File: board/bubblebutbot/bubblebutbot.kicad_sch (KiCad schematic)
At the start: 23 parts, among them J1 Screw_Terminal_01x02, J2 Screw_Terminal_01x02, J3 Conn_01x06_Female, J4 Conn_01x06_Female, J5 Screw_Terminal_01x02, J6 Screw_Terminal_01x02, Q1 FDN336P, U1 WeMos_D1_mini, U3 TPS613222ADBV

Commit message: gerber for 1v01 ready
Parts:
- removed J1, J2, J5, J6: Screw_Terminal_01x02, TerminalBlock:TerminalBlock_bornier-2_P5.08mm, symbol Connector:Screw_Terminal_01x02
- added J1, J2: Screw_Terminal_01x04, TerminalBlock_MetzConnect:TerminalBlock_MetzConnect_Type094_RT03504HBLU_1x04_P5.00mm_Horizontal, symbol Connector:Screw_Terminal_01x04
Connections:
- net GND: now also J1.1 (Pin_1)
- net SERVO_PWM: now also J1.3 (Pin_3)
- net SPLY: now also J1.4 (Pin_4)
- net at L1.1, R3.1: now also J1.2 (Pin_2)
- net at J3.3 (Pin_3): now also J2.3 (Pin_3)
- net at J3.2 (Pin_2): now also J2.4 (Pin_4)
- net at J3.4 (Pin_4): now also J2.2 (Pin_2)
- net at J3.5 (Pin_5): now also J2.1 (Pin_1)

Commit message: first steps into the final prod pcb!
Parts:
- removed C4: 10u, Capacitor_SMD:C_0603_1608Metric_Pad1.08x0.95mm_HandSolder, symbol Device:C
- removed D1: SS14, Diode_SMD:D_SMA, symbol Device:D_Schottky
- removed D3: LED, LED_SMD:LED_0603_1608Metric_Pad1.05x0.95mm_HandSolder, symbol Device:LED
- removed J1, J2: Screw_Terminal_01x04, TerminalBlock_MetzConnect:TerminalBlock_MetzConnect_Type094_RT03504HBLU_1x04_P5.00mm_Horizontal, symbol Connector:Screw_Terminal_01x04
- removed J3, J4: Conn_01x06_Female, Connector_PinSocket_2.54mm:PinSocket_1x06_P2.54mm_Vertical, symbol Connector:Conn_01x06_Female
- removed L1: 2.2u, Inductor_SMD:L_Coilcraft_LPS4018, symbol Device:L
- removed R3: 10k, Resistor_SMD:R_0603_1608Metric_Pad0.98x0.95mm_HandSolder, symbol Device:R
- removed R4: 33k, Resistor_SMD:R_0603_1608Metric_Pad0.98x0.95mm_HandSolder, symbol Device:R
- removed U1: WeMos_D1_mini, Module:WEMOS_D1_mini_light, symbol MCU_Module:WeMos_D1_mini
- removed U3: TPS613222ADBV, Package_TO_SOT_SMD:SOT-23-5, symbol Regulator_Switching:TPS613222ADBV
- added D1: LED, symbol Device:LED
- added J1: JST XH, symbol Connector:Conn_01x02_Socket
- added SW1, SW2: SW_SPST, symbol Switch:SW_SPST
- added U1: MPU-6050, Sensor_Motion:InvenSense_QFN-24_4x4mm_P0.5mm, symbol Sensor_Motion:MPU-6050
- added U2: ESP32-S3-WROOM-1, Espressif:ESP32-S3-WROOM-1, symbol PCM_Espressif:ESP32-S3-WROOM-1
- C1: value 120p -> 10u; LCSC C1643 -> C380316
- C2, C3: LCSC C19702 -> C380316
- R1: value 5 -> 5.1K; footprint Resistor_SMD:R_0805_2012Metric_Pad1.20x1.40mm_HandSolder -> (none); LCSC C17724 -> C2907114; descp 5 OHM 5% 1/3W 0805 -> (none)
- R2: value 1k -> 5.1K; footprint Resistor_SMD:R_0603_1608Metric_Pad0.98x0.95mm_HandSolder -> (none); LCSC C21190 -> C2907114
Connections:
- net GND: now also C1.2, D1.1 (K), J1.1 (Pin_1), SW1.2 (B), SW2.2 (B), U2.1 (GND), U2.40 (GND), U2.41 (GND)
- net ESP32-OP-LED: now reaches R2.2
- net ESP32-OP-LED: now also U2.21 (GPIO13/TOUCH13/ADC2_CH2/FSPIQ/FSPIIO7/SUBSPIQ)
- net +3.3V: now reaches R1.1
- net +3.3V: now also C1.1, C2.1, U2.2 (3V3)
- net ESP32-RESET: now reaches R1.2
- net ESP32-RESET: now also C3.1, SW2.1 (A), U2.3 (EN); no longer C1.1
- net at R2.1: now also D1.2 (A)
- new net +7.5V: J1.2 (Pin_2)
- new net ESP32-BOOT0: SW1.1 (A), U2.27 (GPIO0/BOOT)
- now unconnected: Q1.2 (S)
- no-connect marks 9 -> 0
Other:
- note added: "ESP32-S3-WROOM-1-N8: https://www.lcsc.com/product-detail/WiFi-Modules_Espressif-Systems-ESP32-S3-WROOM-1-N8_C2913198.html"
- note added: "JST XH: https://www.lcsc.com/product-detail/Wire-To-Board-Wire-To-Wire-Connector_BOOMELE-Boom-Precision-Elec-XH-2AW_C33132.html"
- note removed: "BATTERY"
- note removed: "Battery has no protection so be careful!"
- note removed: "MOTOR DRIVER"
- note removed: "OK"
- note removed: "SERVO TERMINAL"
- note removed: "TO 5V BOOST"
- note removed: "WEMOS D1 BOARD"
- moved on the sheet: D2, Q1

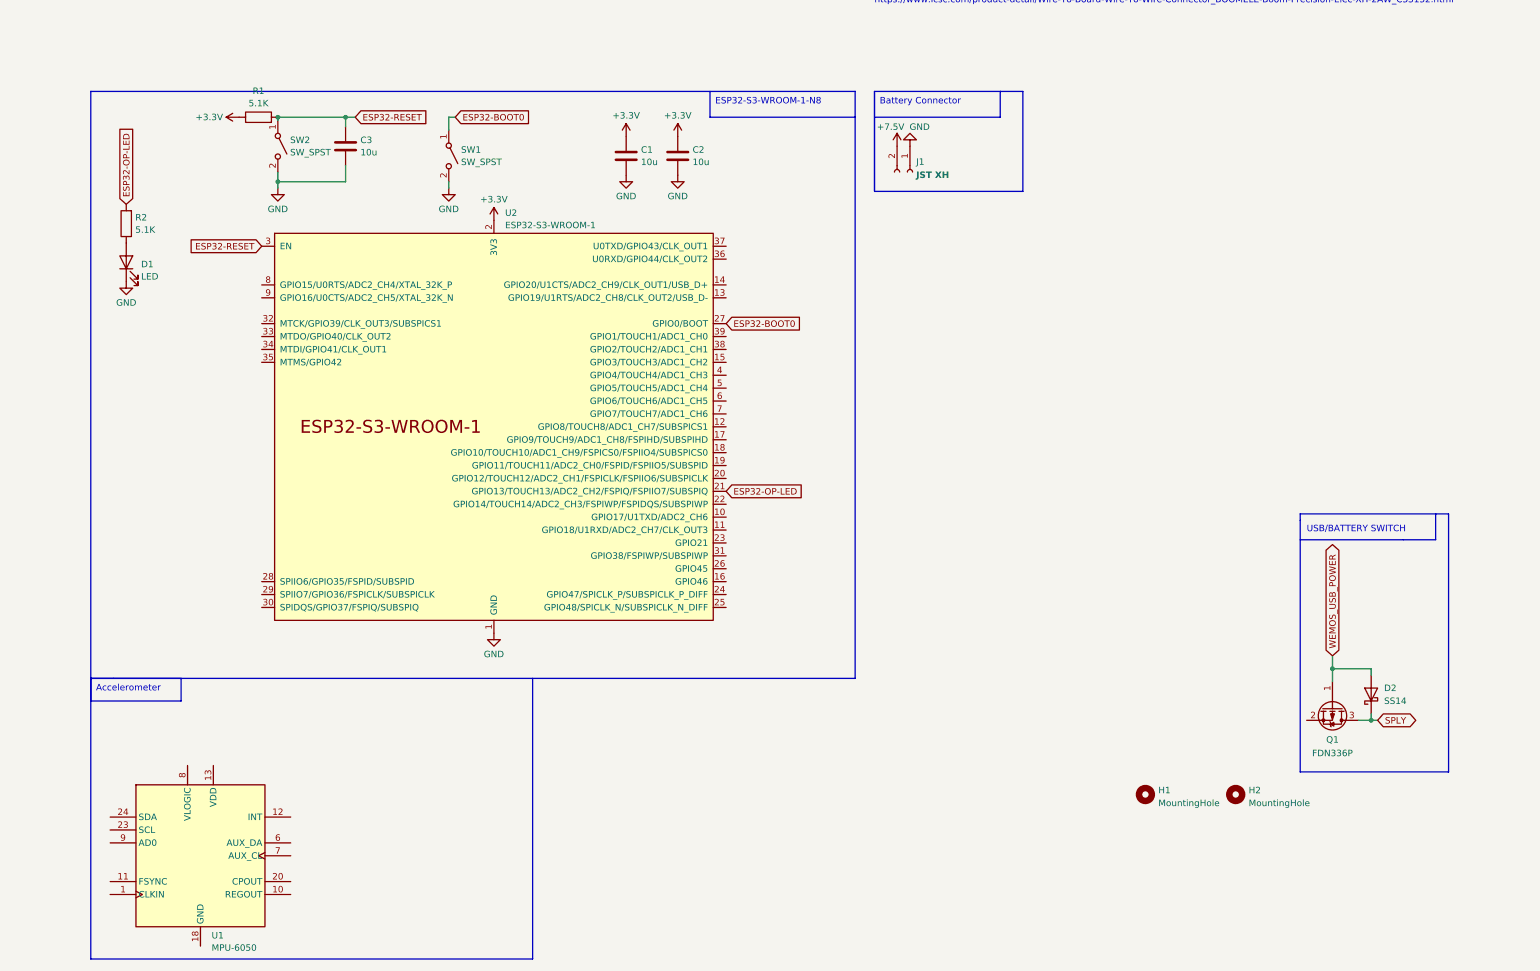
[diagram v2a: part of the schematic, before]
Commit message: added acc and 3v3 buck
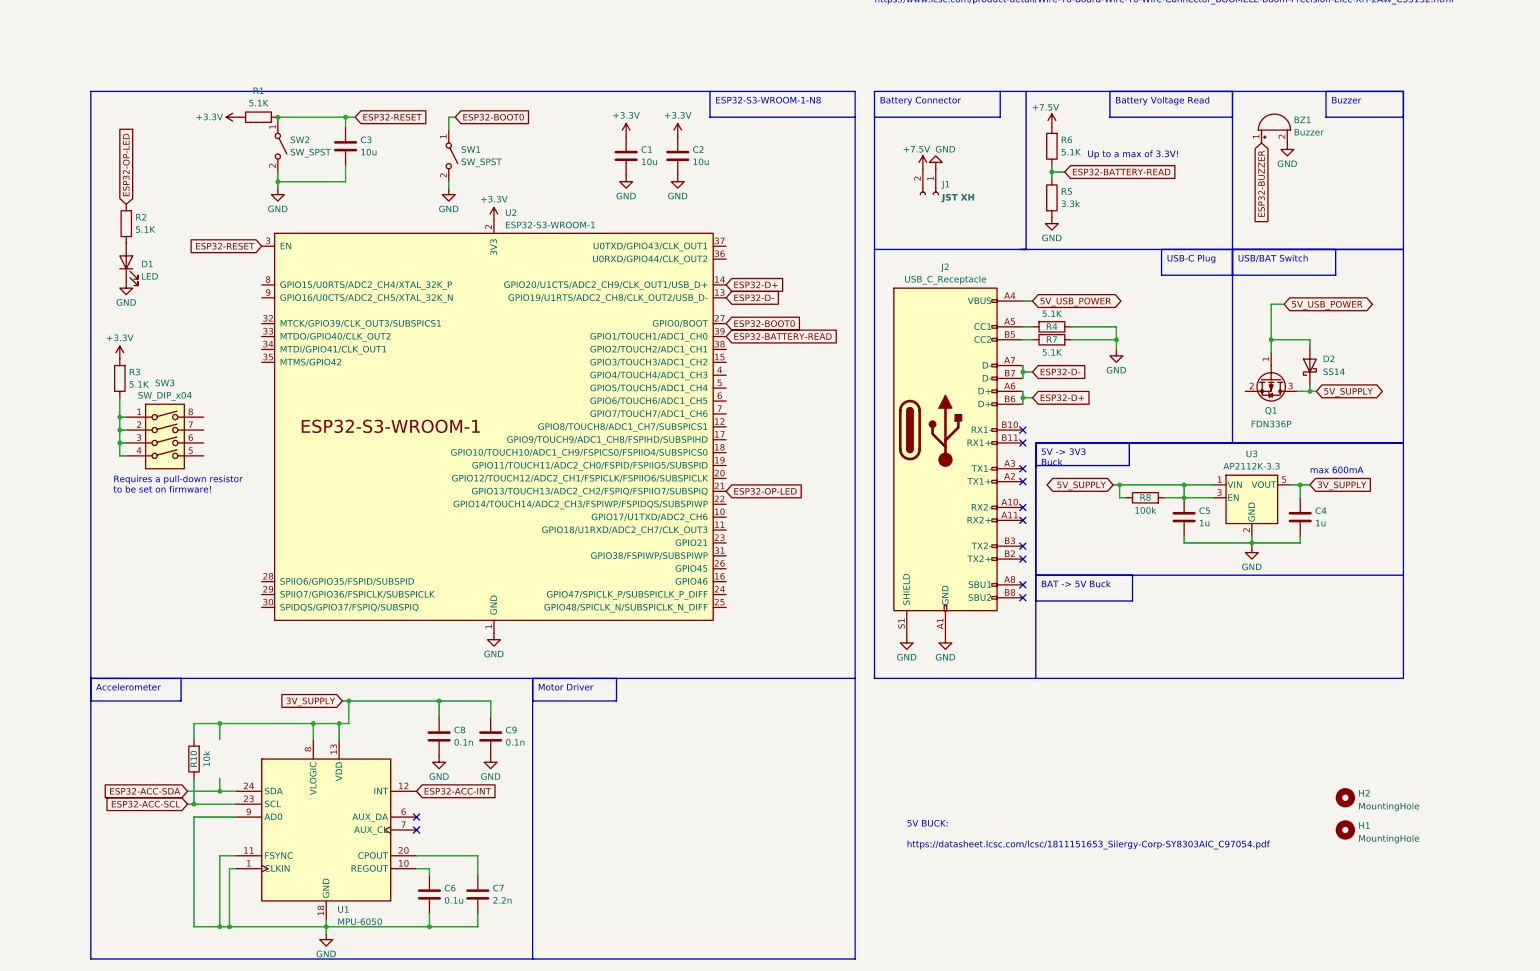
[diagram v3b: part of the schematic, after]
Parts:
- added BZ1: Buzzer, Buzzer_Beeper:MagneticBuzzer_PUI_AT-0927-TT-6-R, symbol Device:Buzzer
- added C4, C5: 1u, symbol Device:C
- added C6: 0.1u, Capacitor_SMD:C_0603_1608Metric_Pad1.08x0.95mm_HandSolder, symbol Device:C
- added C7: 2.2n, Capacitor_SMD:C_0603_1608Metric_Pad1.08x0.95mm_HandSolder, symbol Device:C
- added C8, C9: 0.1n, Capacitor_SMD:C_0603_1608Metric_Pad1.08x0.95mm_HandSolder, symbol Device:C
- added J2: USB_C_Receptacle, Connector_USB:USB_C_Receptacle_GCT_USB4105-xx-A_16P_TopMnt_Horizontal, symbol Connector:USB_C_Receptacle
- added R10: 10k, symbol Device:R
- added R3: 5.1K, Resistor_SMD:R_0603_1608Metric_Pad0.98x0.95mm_HandSolder, symbol Device:R
- added R4, R6, R7: 5.1K, symbol Device:R
- added R5: 3.3k, Resistor_SMD:R_0603_1608Metric_Pad0.98x0.95mm_HandSolder, symbol Device:R
- added R8: 100k, Resistor_SMD:R_0603_1608Metric_Pad0.98x0.95mm_HandSolder, symbol Device:R
- added SW3: SW_DIP_x04, Button_Switch_THT:SW_DIP_SPSTx04_Piano_10.8x11.72mm_W7.62mm_P2.54mm, symbol Switch:SW_DIP_x04
- added U3: AP2112K-3.3, Package_TO_SOT_SMD:SOT-23-5, symbol Regulator_Linear:AP2112K-3.3
- D1: footprint (none) -> LED_SMD:LED_0603_1608Metric_Pad1.05x0.95mm_HandSolder; LCSC (none) -> C965799
- R1, R2: footprint (none) -> Resistor_SMD:R_0603_1608Metric_Pad0.98x0.95mm_HandSolder
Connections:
- net +3.3V: now also R3.2
- net +7.5V: now also R6.2
- net GND: now also U1.1 (CLKIN), U1.11 (FSYNC), U1.18 (GND), U1.9 (AD0), BZ1.2 (+), C4.2, C5.2, C6.2, C7.2, C8.2, C9.2, J2.A1 (GND), J2.A12 (GND), J2.B1 (GND), J2.B12 (GND), J2.S1 (SHIELD), R4.1, R5.2, R7.2, U3.2 (GND)
- net at U1.10 (REGOUT): now also C6.1
- net ESP32-ACC-INT: now reaches U1.12 (INT)
- net 3V_SUPPLY: now reaches U1.13 (VDD)
- net 3V_SUPPLY: now also U1.8 (VLOGIC), C4.1, C8.1, C9.1, R10.2, U3.5 (VOUT)
- net at U1.20 (CPOUT): now also C7.1
- net ESP32-ACC-SCL: now reaches U1.23 (SCL)
- net ESP32-ACC-SCL: now also R10.1
- net ESP32-ACC-SDA: now reaches U1.24 (SDA)
- net ESP32-D-: now reaches U2.13 (GPIO19/U1RTS/ADC2_CH8/CLK_OUT2/USB_D-)
- net ESP32-D-: now also J2.A7 (D-), J2.B7 (D-)
- net ESP32-D+: now reaches U2.14 (GPIO20/U1CTS/ADC2_CH9/CLK_OUT1/USB_D+)
- net ESP32-D+: now also J2.A6 (D+), J2.B6 (D+)
- net ESP32-BATTERY-READ: now reaches U2.39 (GPIO1/TOUCH1/ADC1_CH0)
- net ESP32-BATTERY-READ: now also R5.1, R6.1
- net SPLY renamed 5V_SUPPLY
- net 5V_SUPPLY: now also C5.1, R8.1, R8.2, U3.1 (VIN), U3.3 (EN)
- net WEMOS_USB_POWER renamed 5V_USB_POWER
- net 5V_USB_POWER: now also J2.A4 (VBUS), J2.A9 (VBUS), J2.B4 (VBUS), J2.B9 (VBUS)
- new net: J2.B5 (CC2), R7.1
- new net: R3.1, SW3.1, SW3.2, SW3.3, SW3.4
- new net: J2.A5 (CC1), R4.2
- new net ESP32-BUZZER: BZ1.1 (-)
- no-connect marks 0 -> 12
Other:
- note added: "5V BUCK: https://datasheet.lcsc.com/lcsc/1811151653_Silergy-Corp-SY8303AIC_C97054.pdf"
- note added: "Requires a pull-down resistor to be set on firmware!"
- note added: "Up to a max of 3.3V!"
- note added: "max 600mA"
- note removed: "USB/BATTERY SWITCH"
- moved on the sheet: D2, H1, H2, J1, Q1, U1

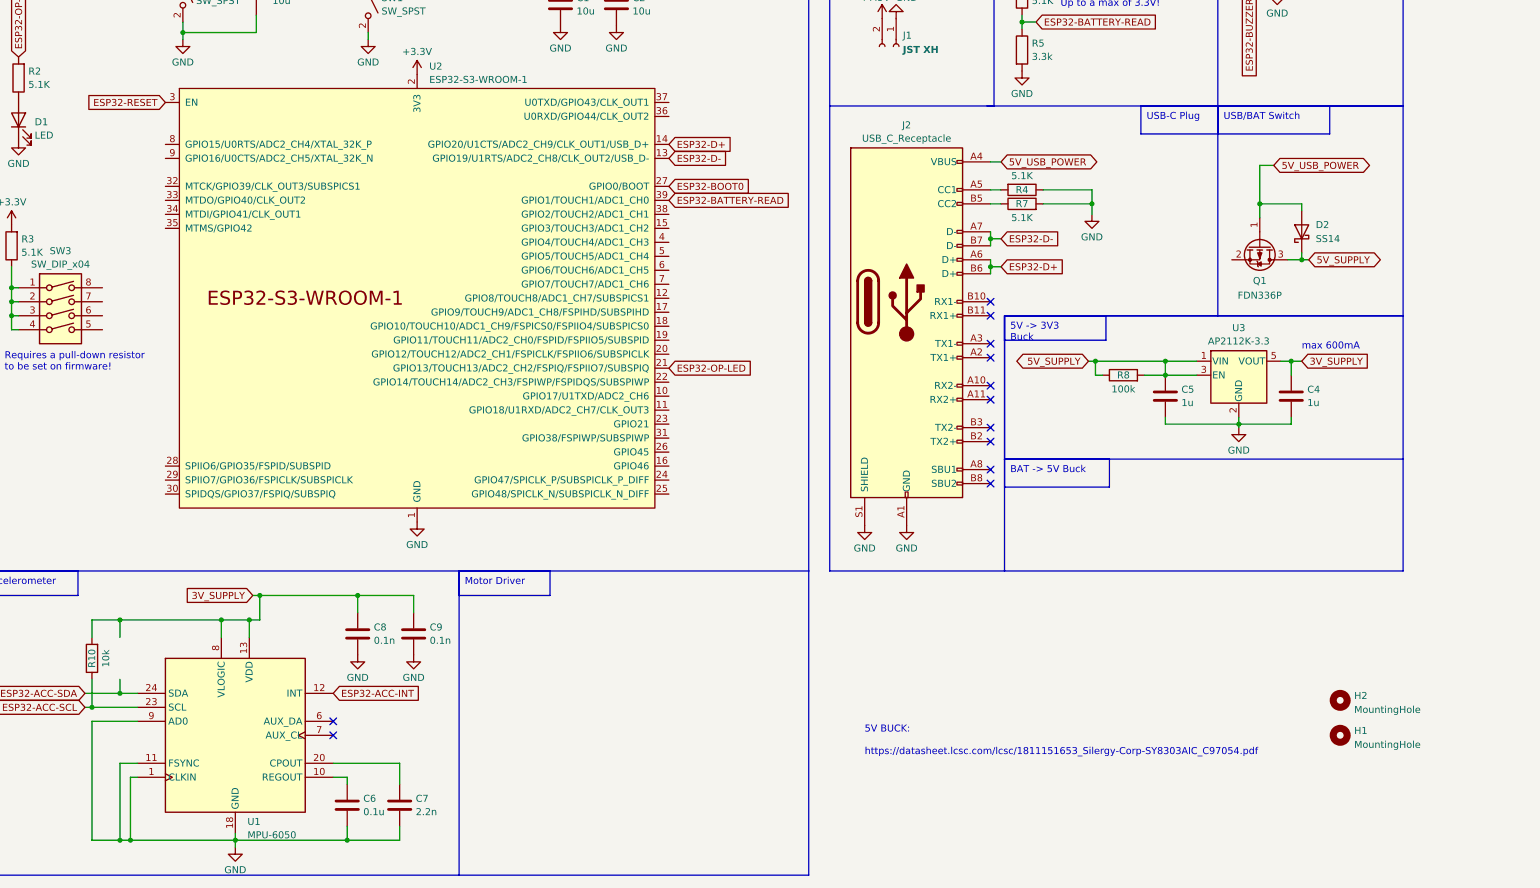
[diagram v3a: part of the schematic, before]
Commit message: Added some more pins and set up the DIPx4
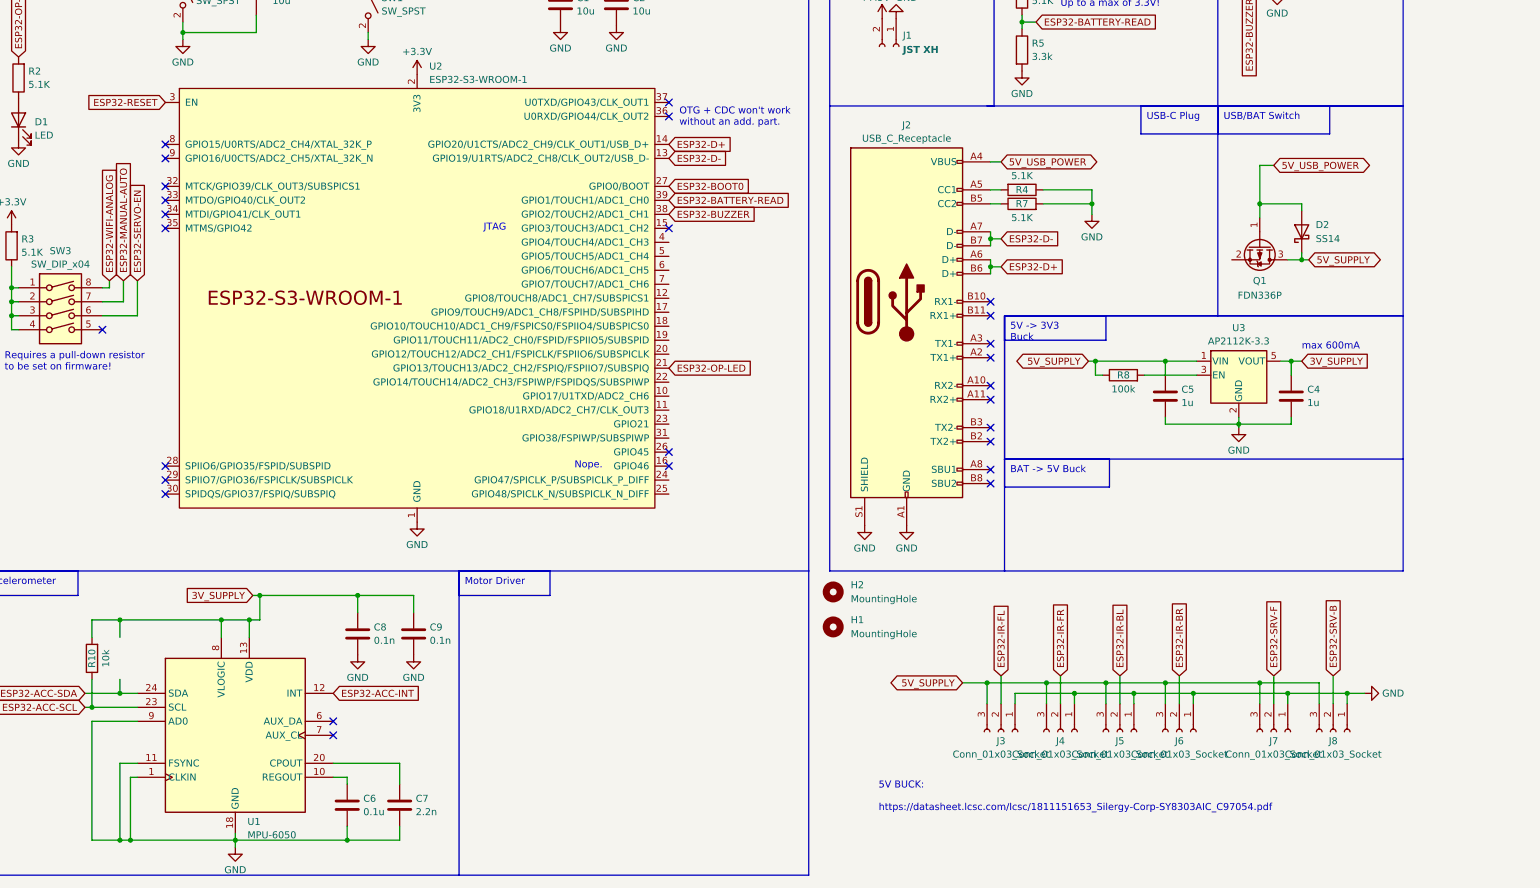
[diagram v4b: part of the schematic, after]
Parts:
- added J3, J4, J5, J6, J7, J8: Conn_01x03_Socket, symbol Connector:Conn_01x03_Socket
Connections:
- net 5V_SUPPLY: now also J3.3 (Pin_3), J4.3 (Pin_3), J5.3 (Pin_3), J6.3 (Pin_3), J7.3 (Pin_3), J8.3 (Pin_3); no longer R8.2, U3.3 (EN)
- net ESP32-BUZZER: now also U2.38 (GPIO2/TOUCH2/ADC1_CH1)
- net GND: now also J3.1 (Pin_1), J4.1 (Pin_1), J5.1 (Pin_1), J6.1 (Pin_1), J7.1 (Pin_1), J8.1 (Pin_1)
- net ESP32-SERVO-EN: now reaches SW3.6
- net ESP32-MANUAL-AUTO: now reaches SW3.7
- net ESP32-WIFI-ANALOG: now reaches SW3.8
- new net: R8.2, U3.3 (EN)
- new net ESP32-IR-BL: J5.2 (Pin_2)
- new net ESP32-IR-BR: J6.2 (Pin_2)
- new net ESP32-IR-FL: J3.2 (Pin_2)
- new net ESP32-IR-FR: J4.2 (Pin_2)
- new net ESP32-SRV-B: J8.2 (Pin_2)
- new net ESP32-SRV-F: J7.2 (Pin_2)
- no-connect marks 12 -> 27
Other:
- note added: "JTAG"
- note added: "Nope."
- note added: "OTG + CDC won't work without an add. part."
- moved on the sheet: H1, H2

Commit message: A few additions: new acc and motor driver schematics.
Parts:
- removed C9: 0.1n, Capacitor_SMD:C_0603_1608Metric_Pad1.08x0.95mm_HandSolder, symbol Device:C
- removed U1: MPU-6050, Sensor_Motion:InvenSense_QFN-24_4x4mm_P0.5mm, symbol Sensor_Motion:MPU-6050
- added C10: 10u, Capacitor_SMD:C_0603_1608Metric_Pad1.08x0.95mm_HandSolder, symbol Device:C
- added J10, J11, J12, J9: JST XH, symbol Connector:Conn_01x02_Socket
- added R11: 50k, Resistor_SMD:R_0603_1608Metric_Pad0.98x0.95mm_HandSolder, symbol Device:R
- added R9: 10k, symbol Device:R
- added U1: DRV8833PWP, Package_SO:HTSSOP-16-1EP_4.4x5mm_P0.65mm_EP3.4x5mm_Mask2.46x2.31mm_ThermalVias, symbol Driver_Motor:DRV8833PWP
- added U4: LIS3DH, Package_LGA:LGA-16_3x3mm_P0.5mm_LayoutBorder3x5y, symbol Sensor_Motion:LIS3DH
- C6: value 0.1u -> 100n; LCSC (none) -> C282519
- C7: value 2.2n -> 2.2u; LCSC (none) -> C2691406
- C8: value 0.1n -> 100n; LCSC (none) -> C282519
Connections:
- net 3V_SUPPLY: now also C6.1, C10.1, R9.2, U4.1 (VDD_IO), U4.14 (VDD); no longer C8.1
- net 5V_SUPPLY: now also C8.2, R11.1, U1.12 (VM)
- net ESP32-ACC-SCL: now also R9.1, U4.4 (SCL/SPC); no longer R10.1
- net ESP32-ACC-SDA: now also R10.1, U4.6 (SDA/SDI/SDO)
- net ESP32-MANUAL-AUTO: now also U2.17 (GPIO9/TOUCH9/ADC1_CH8/FSPIHD/SUBSPIHD)
- net ESP32-SERVO-EN: now also U2.18 (GPIO10/TOUCH10/ADC1_CH9/FSPICS0/FSPIIO4/SUBSPICS0)
- net ESP32-WIFI-ANALOG: now also U2.12 (GPIO8/TOUCH8/ADC1_CH7/SUBSPICS1)
- net GND: now also C10.2, U1.13 (GND), U1.17 (GND(PPAD)), U1.3 (AISEN), U1.6 (BISEN), U4.10 (GND), U4.12 (GND), U4.5 (GND), U4.7 (SDO/SA0); no longer C8.2
- net at C7.1: now also U1.14 (VINT)
- net ESP32-MOTOR-AIN1: now reaches U2.10 (GPIO17/U1TXD/ADC2_CH6)
- net ESP32-MOTOR-AIN1: now also U1.16 (AIN1)
- net ESP32-MOTOR-AIN2: now reaches U2.11 (GPIO18/U1RXD/ADC2_CH7/CLK_OUT3)
- net ESP32-MOTOR-AIN2: now also U1.15 (AIN2)
- net ESP32-ACC-INT1: now reaches U2.19 (GPIO11/TOUCH11/ADC2_CH0/FSPID/FSPIIO5/SUBSPID)
- net ESP32-ACC-INT1: now also U4.11 (INT1)
- net ESP32-ACC-INT2: now reaches U2.20 (GPIO12/TOUCH12/ADC2_CH1/FSPICLK/FSPIIO6/SUBSPICLK)
- net ESP32-ACC-INT2: now also U4.9 (INT2)
- net ESP32-MOTOR-FAULT: now reaches U2.22 (GPIO14/TOUCH14/ADC2_CH3/FSPIWP/FSPIDQS/SUBSPIWP)
- net ESP32-MOTOR-FAULT: now also U1.8 (nFAULT)
- net ESP32-MOTOR-BIN1: now reaches U2.23 (GPIO21)
- net ESP32-MOTOR-BIN1: now also U1.9 (BIN1)
- net ESP32-MOTOR-BIN2: now reaches U2.31 (GPIO38/FSPIWP/SUBSPIWP)
- net ESP32-MOTOR-BIN2: now also U1.10 (BIN2)
- new net: R11.2, U1.1 (nSLEEP)
- new net: C8.1, U1.11 (VCP)
- new net MOTOR-LEFT-BL: J10.1 (Pin_1), J9.1 (Pin_1), U1.7 (BOUT1)
- new net MOTOR-LEFT-BR: J10.2 (Pin_2), J9.2 (Pin_2), U1.5 (BOUT2)
- new net MOTOR-RIGHT-BL: J11.1 (Pin_1), J12.1 (Pin_1), U1.2 (AOUT1)
- new net MOTOR-RIGHT-BR: J11.2 (Pin_2), J12.2 (Pin_2), U1.4 (AOUT2)
- no-connect marks 27 -> 29
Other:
- note added: "Design example of the LIS3DH: https://cdn.sparkfun.com/datasheets/Sensors/Accelerometers/ SparkFun_LIS3DH-Breakout.pdf?_gl=1*87mccp*_ga*MjA1MDY4MTg4NC4xNjg4ODM3Nzc3*_ga_T369JS7J9N*MTY5MTMzNjkzNi43LjEuMTY5MTMzODU4Mi42MC4wLjA."
- note added: "FL, e.g. front left. BR, e.g. back right."
- moved on the sheet: D2, H1, H2, J3, J4, J5, J6, J7, J8, Q1, R10
